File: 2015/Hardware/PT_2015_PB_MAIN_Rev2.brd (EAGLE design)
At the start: 142.2 x 170.8 mm, 142 parts, among them Q1 Q_ACS711LC_SKETCH, Q11 Q_IRFS7437PbF, Q12 2N7002, Q14 Q_IRFS7437PbF, Q16 Q_IRFS7437PbF, Q18 Q_FDT86102LZ, Q20 Q_IRFS7437PbF, Q4 Q_ACS711LC, Q5 Q_ACS711LC, Q6 Q_IRFS7437PbF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

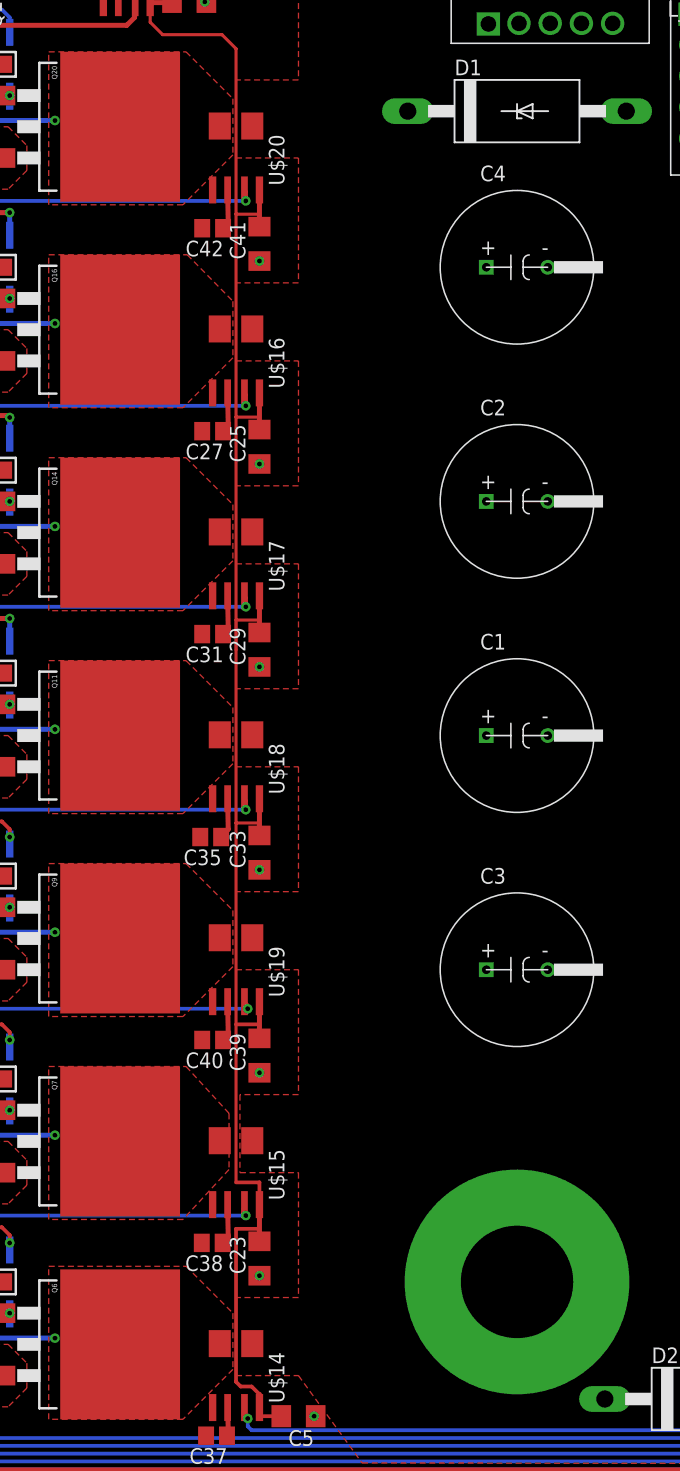
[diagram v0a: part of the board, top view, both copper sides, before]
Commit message: Soldermask removed
high current traces now have soldermask removed to thicken with solder
for higher current capability. Must be coated with solder mask or tape
after soldering. Need to check/verify doing this under the board mount
connectors, diode, and caps using 1oz board - recommend using this
revision to purchase 1oz board for testing.  Final version will be 2oz.
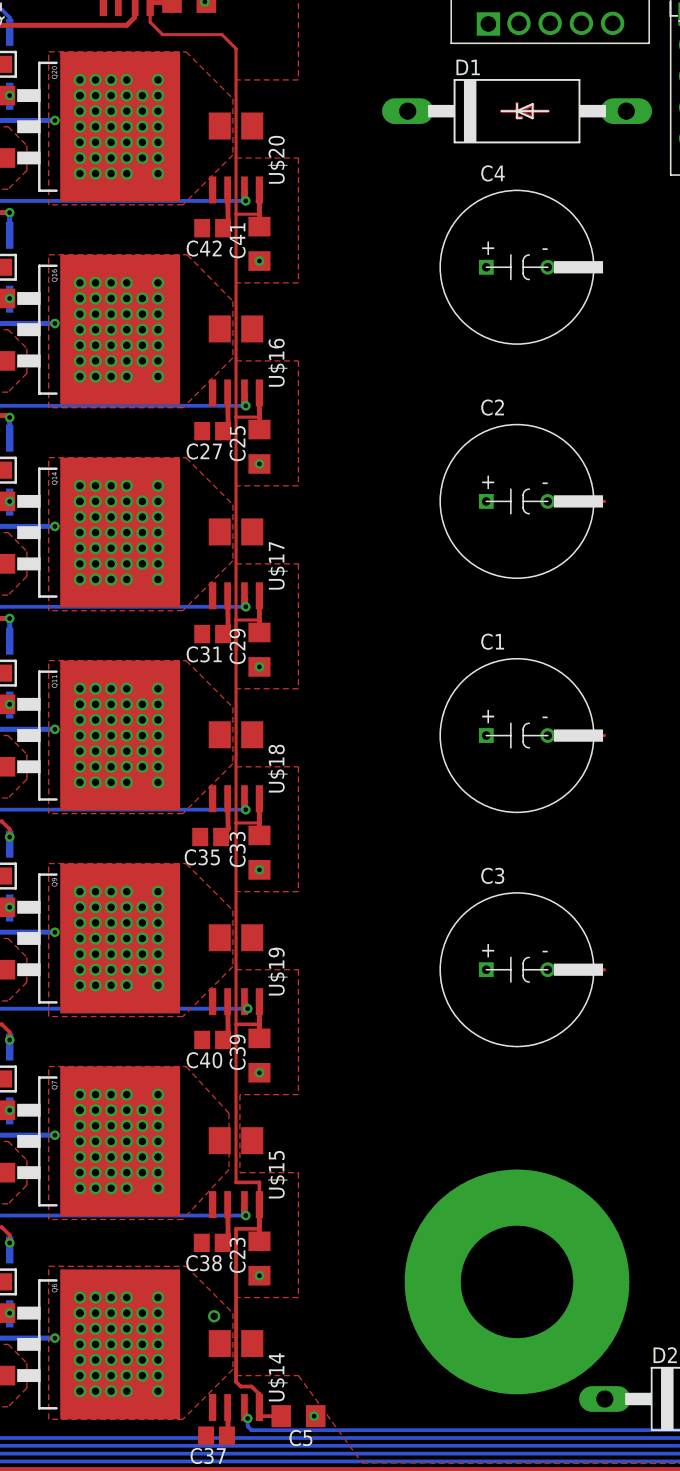
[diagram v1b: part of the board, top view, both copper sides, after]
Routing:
- net N$33: track 0.00 -> 10.2 mm
- net N$43: track 0.00 -> 1.52 mm
- net N$34: track 0.00 -> 1.40 mm
- net N$38: track 0.00 -> 1.40 mm
- net N$37: track 0.00 -> 1.40 mm
- net N$40: vias 1 -> 2
